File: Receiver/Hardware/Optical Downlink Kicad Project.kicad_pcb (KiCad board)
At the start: 2 copper layers, 18 parts, among them J1 Conn_01x20_Socket, J2 Conn_01x20_Socket, U1 OPA657U, U2 TLE2426-EP_D_8, U3 OPA657U, U4 ADS8691IPWR, U5 MEV3S0515SC, U6 LM2940IMPX-8.0/NOPB

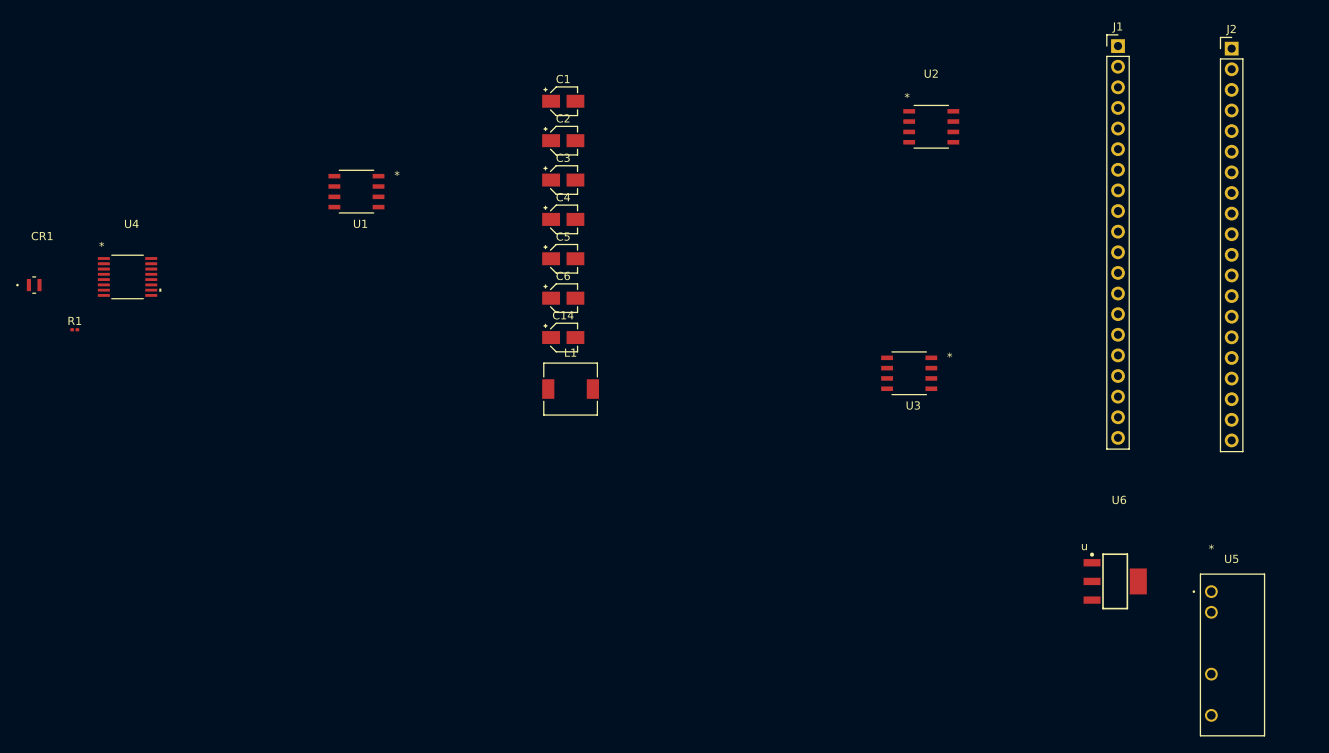
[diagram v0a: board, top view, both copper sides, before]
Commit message: Made some Symbol Changes
Have to change LDO and Boost Converter to components more accessible on JLC PCB.
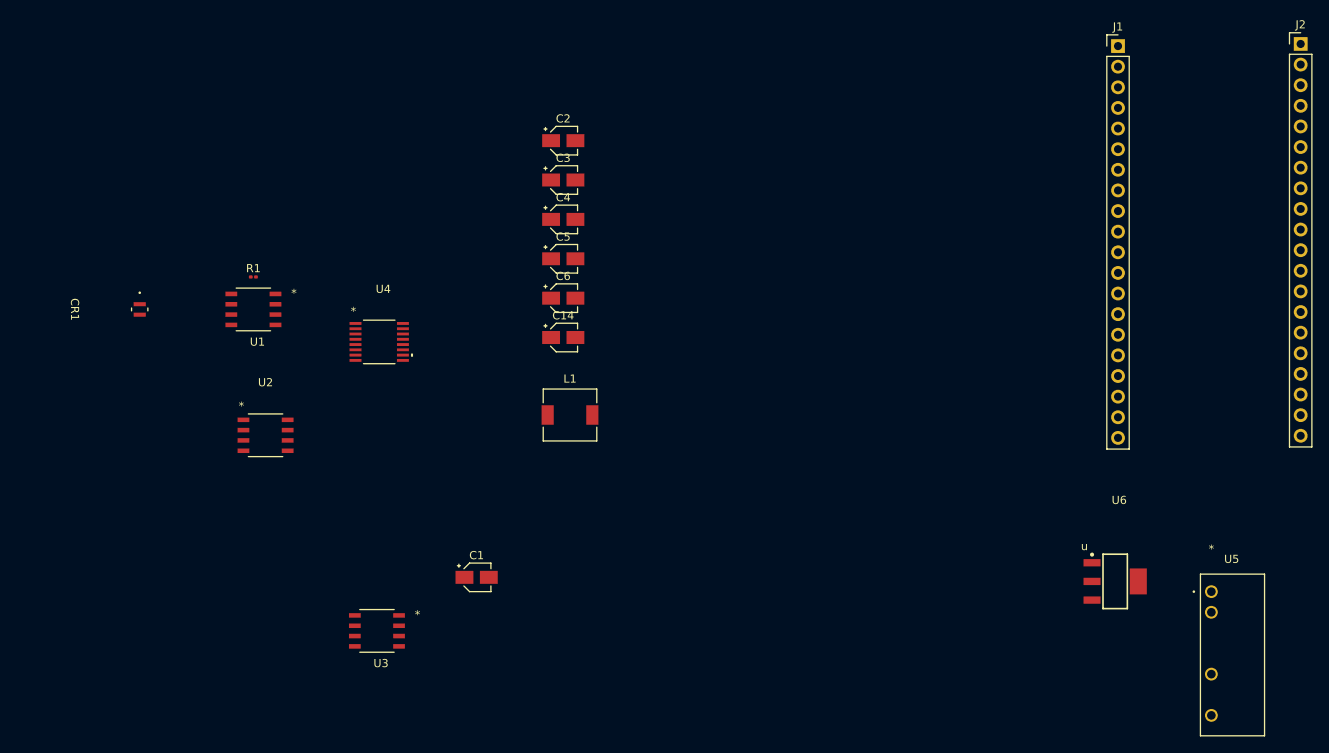
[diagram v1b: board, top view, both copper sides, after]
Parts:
- moved U2 90.4 mm to (70.0, 91.0)
- moved U3 72.8 mm to (83.7, 115.1)
- moved C1 59.6 mm to (96.0, 108.5)
- moved U4 32.0 mm to (84.0, 79.5)
- moved R1 22.9 mm to (68.5, 71.5)
- moved U1 19.3 mm to (68.5, 75.5)
- moved CR1 13.3 mm to (54.5, 75.5), turned to -90 degrees
- moved J2 8.52 mm to (197.5, 42.8)
- moved L1 3.19 mm to (107.5, 88.5)
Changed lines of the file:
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@@
 	(footprint "00-footprint-library:OPA 657 D8"
 		(layer "F.Cu")
-		(at 149.278652 83.365)
+		(at 83.721348 115.095)
 		(tags "OPA657U ")
 		(property "Reference" "U3"
@@
 	(footprint "Resistor_SMD:R_0201_0603Metric"
 		(layer "F.Cu")
-		(at 46.5 78)
+		(at 68.5 71.5)
 		(descr "Resistor SMD 0201 (0603 Metric), square (rectangular) end terminal, IPC-7351 nominal, (Body size source: https://www.vishay.com/docs/20052/crcw0201e3.pdf), generated with kicad-footprint-generator")
 		(tags "resistor")
@@
 		)
 		(property "Value" "15k"
-			(at 0 1.05 0)
+			(at 2.5 -1 0)
 			(layer "F.Fab")
 			(effects
@@
 	(footprint "Capacitor_SMD:CP_Elec_3x5.3"
 		(layer "F.Cu")
-		(at 106.67 49.86)
+		(at 96 108.5)
 		(descr "SMT capacitor, aluminium electrolytic, 3x5.3, Cornell Dubilier Electronics ")
 		(tags "Capacitor Electrolytic")
@@
 	(footprint "Inductor_SMD:L_6.3x6.3_H3"
 		(layer "F.Cu")
-		(at 107.57 85.31)
+		(at 107.5 88.5)
 		(descr "Choke, SMD, 6.3x6.3mm 3mm height")
 		(tags "Choke SMD")
@@
 	(footprint "00-footprint-library:ADS8691IPWR_TEX"
 		(layer "F.Cu")
-		(at 53 71.5)
+		(at 84 79.5)
 		(tags "ADS8691IPWR ")
 		(property "Reference" "U4"
@@
 		)
 		(property "Value" "ADS8691IPWR"
-			(at 0 -8 0)
+			(at 0.579 -3.5 0)
 			(unlocked yes)
 			(layer "F.Fab")
@@
 	(footprint "00-footprint-library:D8_TEX TLE2426-EP_D_8"
 		(layer "F.Cu")
-		(at 152 53)
+		(at 70 91)
 		(tags "TLE2426-EP_D_8 ")
 		(property "Reference" "U2"
@@
 		)
 		(property "Value" "TLE2426-EP_D_8"
-			(at -0.5 -9 0)
+			(at 0 4 0)
 			(unlocked yes)
 			(layer "F.Fab")
@@
 	(footprint "Connector_PinHeader_2.54mm:PinHeader_1x20_P2.54mm_Vertical"
 		(layer "F.Cu")
-		(at 189 43.375)
+		(at 197.5 42.8)
 		(descr "Through hole straight pin header, 1x20, 2.54mm pitch, single row")
 		(tags "Through hole pin header THT 1x20 2.54mm single row")
@@
 	(footprint "00-footprint-library:FR4_C30737MH_EXT"
 		(layer "F.Cu")
-		(at 41.5 72.5)
+		(at 54.5 75.5 -90)
 		(tags "C30737MH-500-90C ")
 		(property "Reference" "CR1"
-			(at 1 -6 0)
+			(at 0 8 270)
 			(unlocked yes)
 			(layer "F.SilkS")
@@
 		)
 		(property "Value" "C30737MH-500-90C"
-			(at 0 -2 0)
+			(at -0.5 4 270)
 			(unlocked yes)
 			(layer "F.Fab")
@@
 		)
 		(property "Datasheet" "C30737MH-500-90C"
-			(at 0 0 0)
+			(at 0 0 90)
 			(layer "F.Fab")
 			(hide yes)
@@
 		)
 		(property "Description" ""
-			(at 0 0 0)
+			(at 0 0 90)
 			(layer "F.Fab")
 			(hide yes)
@@
 		)
 		(fp_line
-			(start -1.2573 -1.1303)
-			(end 1.2573 -1.1303)
+			(start -1.2573 1.1303)
+			(end -1.2573 1.0033)
 			(stroke
 				(width 0.1524)
@@
 		)
 		(fp_line
-			(start -1.2573 -1.0033)
-			(end -1.2573 -1.1303)
+			(start 1.2573 1.1303)
+			(end -1.2573 1.1303)
 			(stroke
 				(width 0.1524)
@@
 		)
 		(fp_line
-			(start -1.2573 -1.0033)
-			(end -1.2573 -1.0033)
+			(start -1.2573 1.0033)
+			(end -1.2573 1.0033)
 			(stroke
 				(width 0.1524)
@@
 		)
 		(fp_line
-			(start -1.2573 1.0033)
-			(end -1.2573 1.0033)
+			(start 1.2573 1.0033)
+			(end 1.2573 1.1303)
 			(stroke
 				(width 0.1524)
@@
 		)
 		(fp_line
-			(start -1.2573 1.1303)
-			(end -1.2573 1.0033)
+			(start 1.2573 1.0033)
+			(end 1.2573 1.0033)
 			(stroke
 				(width 0.1524)
@@
 		)
 		(fp_line
-			(start 1.2573 -1.1303)
-			(end 1.2573 -1.0033)
+			(start -1.2573 -1.0033)
+			(end -1.2573 -1.0033)
 			(stroke
 				(width 0.1524)
@@
 		)
 		(fp_line
-			(start 1.2573 -1.0033)
-			(end 1.2573 -1.0033)
+			(start -1.2573 -1.0033)
+			(end -1.2573 -1.1303)
 			(stroke
 				(width 0.1524)
@@
 		)
 		(fp_line
-			(start 1.2573 1.0033)
-			(end 1.2573 1.0033)
+			(start 1.2573 -1.0033)
+			(end 1.2573 -1.0033)
 			(stroke
 				(width 0.1524)
@@
 		)
 		(fp_line
-			(start 1.2573 1.0033)
-			(end 1.2573 1.1303)
+			(start -1.2573 -1.1303)
+			(end 1.2573 -1.1303)
 			(stroke
 				(width 0.1524)
@@
 		)
 		(fp_line
-			(start 1.2573 1.1303)
-			(end -1.2573 1.1303)
+			(start 1.2573 -1.1303)
+			(end 1.2573 -1.0033)
 			(stroke
 				(width 0.1524)
@@
 		)
 		(fp_line
-			(start -1.0033 -0.8763)
-			(end -1.0033 0.8763)
+			(start -1.0033 0.8763)
+			(end 1.0033 0.8763)
 			(stroke
 				(width 0.0254)
@@
 		)
 		(fp_line
-			(start -1.0033 0.8763)
-			(end 1.0033 0.8763)
+			(start 1.0033 0.8763)
+			(end 1.0033 -0.8763)
 			(stroke
 				(width 0.0254)
@@
 		)
 		(fp_line
-			(start 1.0033 -0.8763)
-			(end -1.0033 -0.8763)
+			(start -1.0033 -0.8763)
+			(end -1.0033 0.8763)
 			(stroke
 				(width 0.0254)
@@
 		)
 		(fp_line
-			(start 1.0033 0.8763)
-			(end 1.0033 -0.8763)
+			(start 1.0033 -0.8763)
+			(end -1.0033 -0.8763)
 			(stroke
 				(width 0.0254)
@@
 		)
 		(fp_text user "${REFERENCE}"
-			(at 0.5 -4 0)
+			(at 0 6 270)
 			(unlocked yes)
 			(layer "F.Fab")
@@
 		)
 		(pad "1" smd rect
-			(at -0.6477 0)
+			(at -0.6477 0 270)
 			(size 0.508 1.4986)
 			(layers "F.Cu" "F.Mask" "F.Paste")
@@
 		)
 		(pad "2" smd rect
-			(at 0.6477 0)
+			(at 0.6477 0 270)
 			(size 0.508 1.4986)
 			(layers "F.Cu" "F.Mask" "F.Paste")
@@
 	(footprint "00-footprint-library:OPA 657 D8"
 		(layer "F.Cu")
-		(at 81.199652 60.990001)
+		(at 68.5 75.5)
 		(tags "OPA657U ")
 		(property "Reference" "U1"
@@
 		)
 		(property "Value" "OPA657U"
-			(at 0.5 -7 0)
+			(at 0.5 6 0)
 			(unlocked yes)
 			(layer "F.Fab")
@@
 		)
 		(fp_text user "${REFERENCE}"
-			(at 0.5 -4 0)
+			(at 0 -0.5 0)
 			(unlocked yes)
 			(layer "F.Fab")

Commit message: Worked on the layout of Optical Downlink
Fixed the layout also added in packages for LDO and boost converter. Need to fix net problems in kicad.
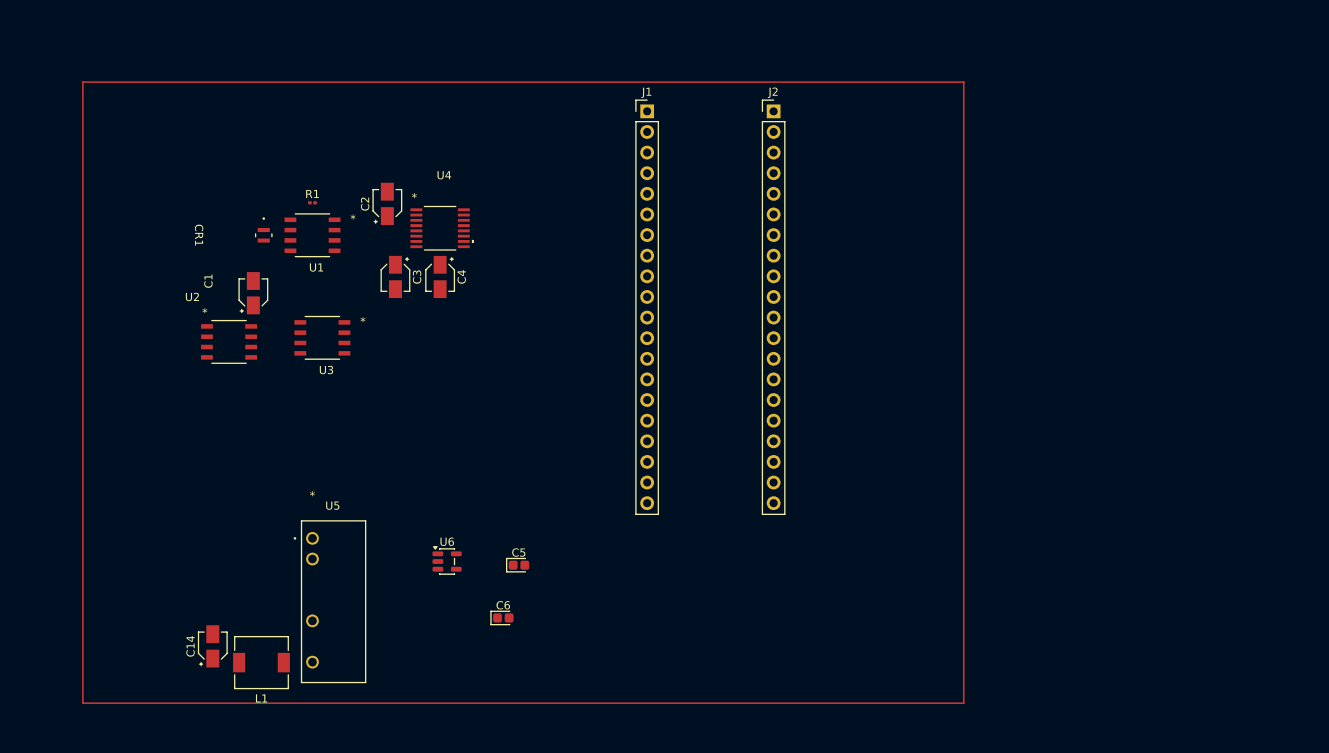
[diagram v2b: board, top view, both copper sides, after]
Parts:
- C5: value 0.47u -> C_Polarized; footprint Capacitor_SMD:CP_Elec_3x5.3 -> Capacitor_Tantalum_SMD:CP_EIA-1608-08_AVX-J
- C6: value 22u -> C_Polarized; footprint Capacitor_SMD:CP_Elec_3x5.3 -> Capacitor_Tantalum_SMD:CP_EIA-1608-08_AVX-J
- U6: value LM2940IMPX-8.0/NOPB -> HT7580-2; footprint 00-footprint-library:LM2940IMPX-8.0_NOPB DCY0004A_N -> Package_TO_SOT_SMD:SOT-23-5
- moved U5 110.9 mm to (75.8, 103.7)
- moved U6 82.3 mm to (92.4, 106.5)
- moved J2 65.4 mm to (132.6, 51.1)
- moved J1 58.6 mm to (117.0, 51.1)
- moved C14 57.5 mm to (63.5, 117.0), turned to 90 degrees
- moved L1 48.7 mm to (69.5, 119.0), turned to 180 degrees
- moved C1 44.5 mm to (68.5, 73.5), turned to 90 degrees
- moved C6 40.1 mm to (99.3, 113.5)
- moved C5 38.1 mm to (101.2, 107.0)
- moved U3 36.7 mm to (77.0, 79.0)
- moved C3 23.9 mm to (86.0, 71.5), turned to -90 degrees
- moved C2 23.0 mm to (85.0, 62.5), turned to 90 degrees
- moved CR1 17.8 mm to (69.8, 66.4)
- moved C4 16.7 mm to (91.5, 71.5), turned to -90 degrees
- moved U4 15.9 mm to (91.5, 65.5)
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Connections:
- C5 pad 1: Net-(U6-IN) -> Net-(U6-Vin)
- C6 pad 1: Net-(U6-OUT) -> Net-(U6-Vout)
- U6 pad 1: Net-(U6-IN) -> (no net)
- U6 pad 2: GND -> (no net)
- U6 pad 3: Net-(U6-OUT) -> (no net)
- U6 pad 4: GND -> (no net)

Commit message: Worked on Assigning capacitor and resistors components
Specifically feedback resistor and worked on capacitor in virtual ground circuit.
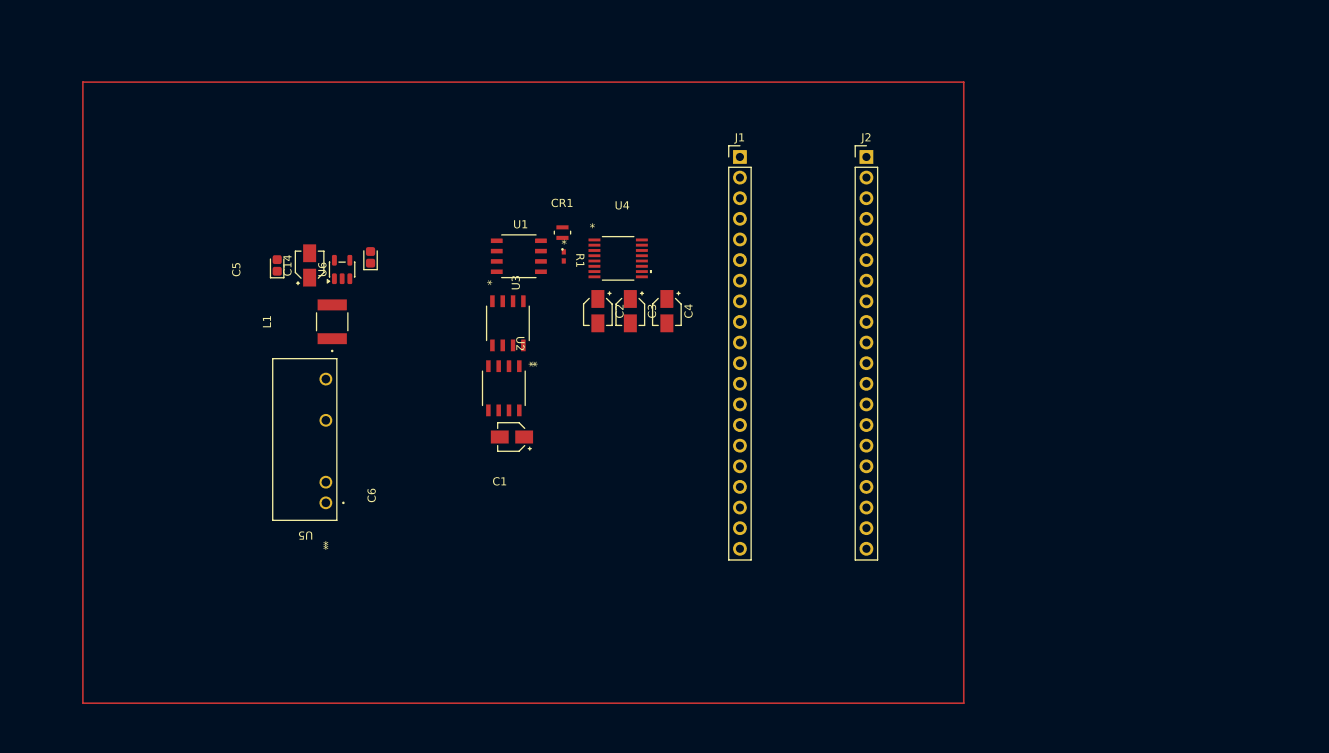
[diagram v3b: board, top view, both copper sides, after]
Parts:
- L1: footprint Inductor_SMD:L_6.3x6.3_H3 -> 00-footprint-library:IND_8400_84XXXC_MUR
- R1: footprint Resistor_SMD:R_0201_0603Metric -> 00-footprint-library:RC0402N_YAG
- moved C14 48.4 mm to (75.4, 70.1)
- moved C5 47.4 mm to (71.4, 70.1), turned to 90 degrees
- moved C6 47.3 mm to (82.9, 69.1), turned to 90 degrees
- moved L1 42.9 mm to (78.2, 77.0), turned to 90 degrees
- moved U6 38.2 mm to (79.4, 70.6), turned to 90 degrees
- moved CR1 36.8 mm to (106.6, 66.0), turned to 90 degrees
- moved C1 36.4 mm to (100.4, 91.2), turned to 180 degrees
- moved U2 34.3 mm to (99.4, 85.2), turned to -90 degrees
- moved R1 31.6 mm to (106.7, 69.0), turned to -90 degrees
- moved C3 29.2 mm to (114.9, 75.7)
- moved C2 29.1 mm to (110.9, 75.7), turned to -90 degrees
- moved C4 28.2 mm to (119.4, 75.7)
- moved U1 25.6 mm to (101.2, 69.0)
- moved U3 22.9 mm to (99.9, 77.2), turned to 90 degrees
- moved U4 22.2 mm to (113.4, 69.2)
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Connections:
- C14 pad 1: Net-(C14-Pad1) -> Intermeditate Power
- C5 pad 1: Net-(U6-Vin) -> Intermeditate Power
- C6 pad 1: Net-(U6-Vout) -> Op Amp Voltage Source
- L1 pad 2: Net-(C14-Pad1) -> Intermeditate Power
- U6 pad 1: (no net) -> GND
- U6 pad 2: (no net) -> Intermeditate Power
- U6 pad 3: (no net) -> Op Amp Voltage Source
- U6 pad 4: (no net) -> unconnected-(U6-NC-Pad4)
- U6 pad 5: (no net) -> unconnected-(U6-NC-Pad5)
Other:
- board text added: "ADC circuit"
- board text added: "Virtual Ground and Tranimpedance amp"
- board text added: "boost converter and LDO"
